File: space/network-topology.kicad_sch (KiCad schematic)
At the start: 14 parts

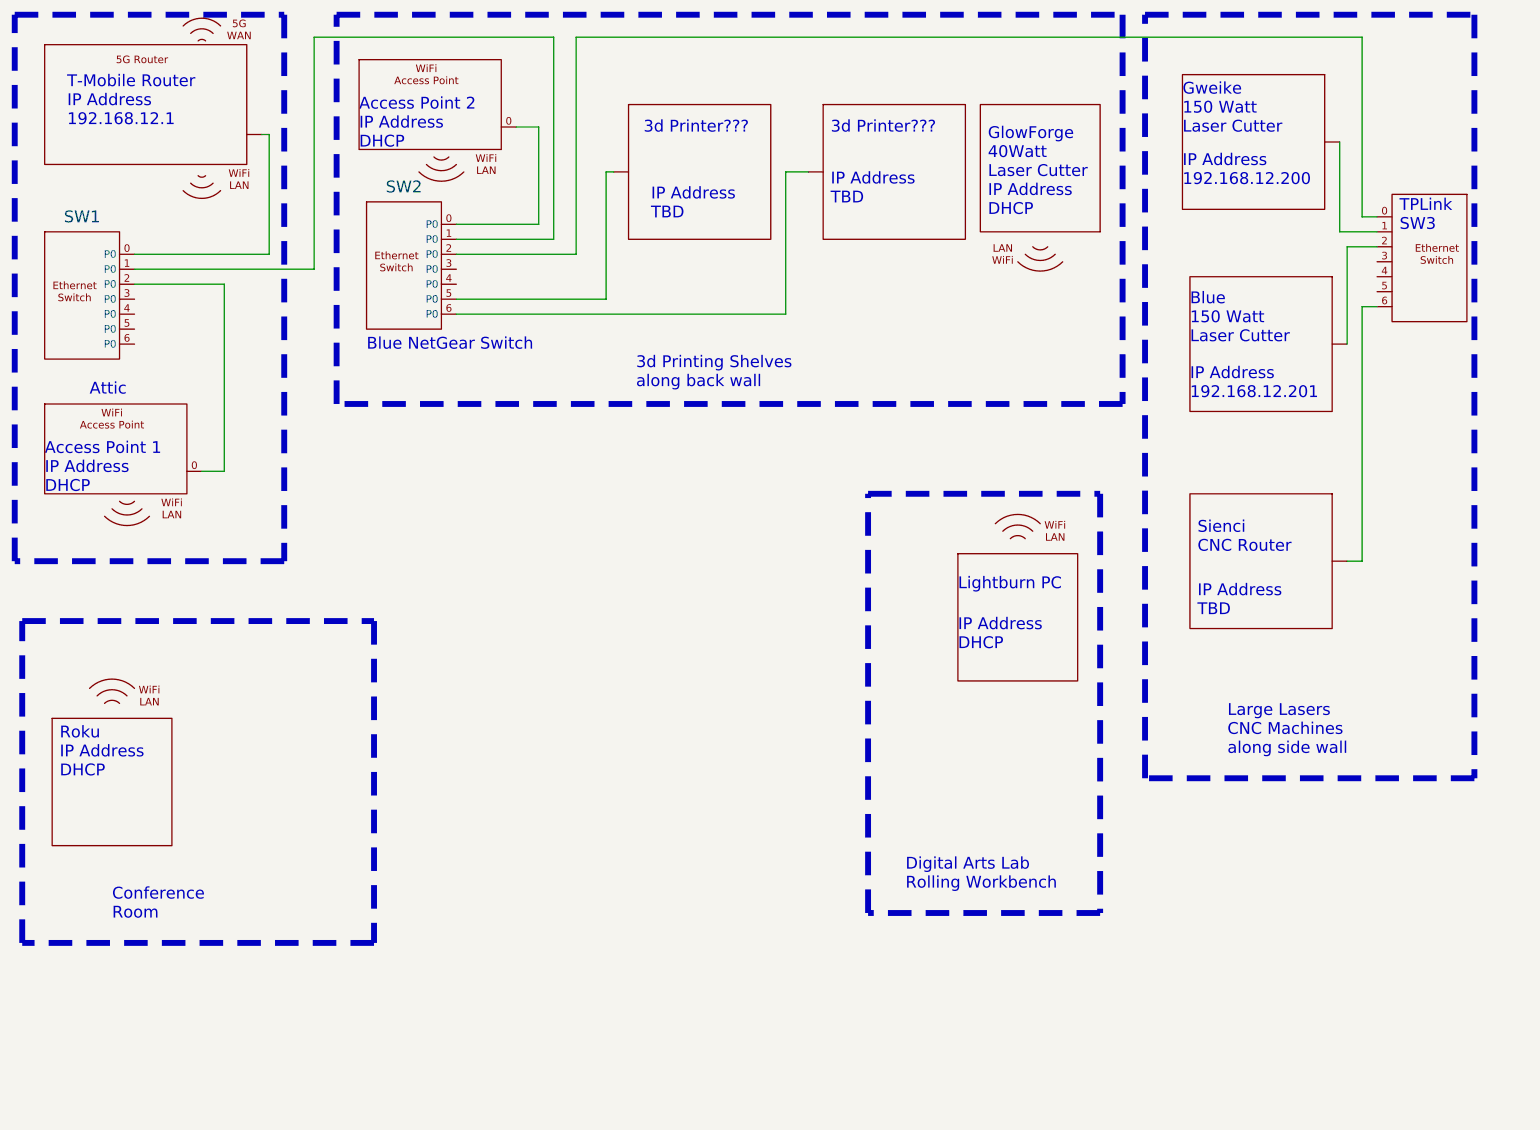
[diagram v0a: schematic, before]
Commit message: Added network map diagrams.
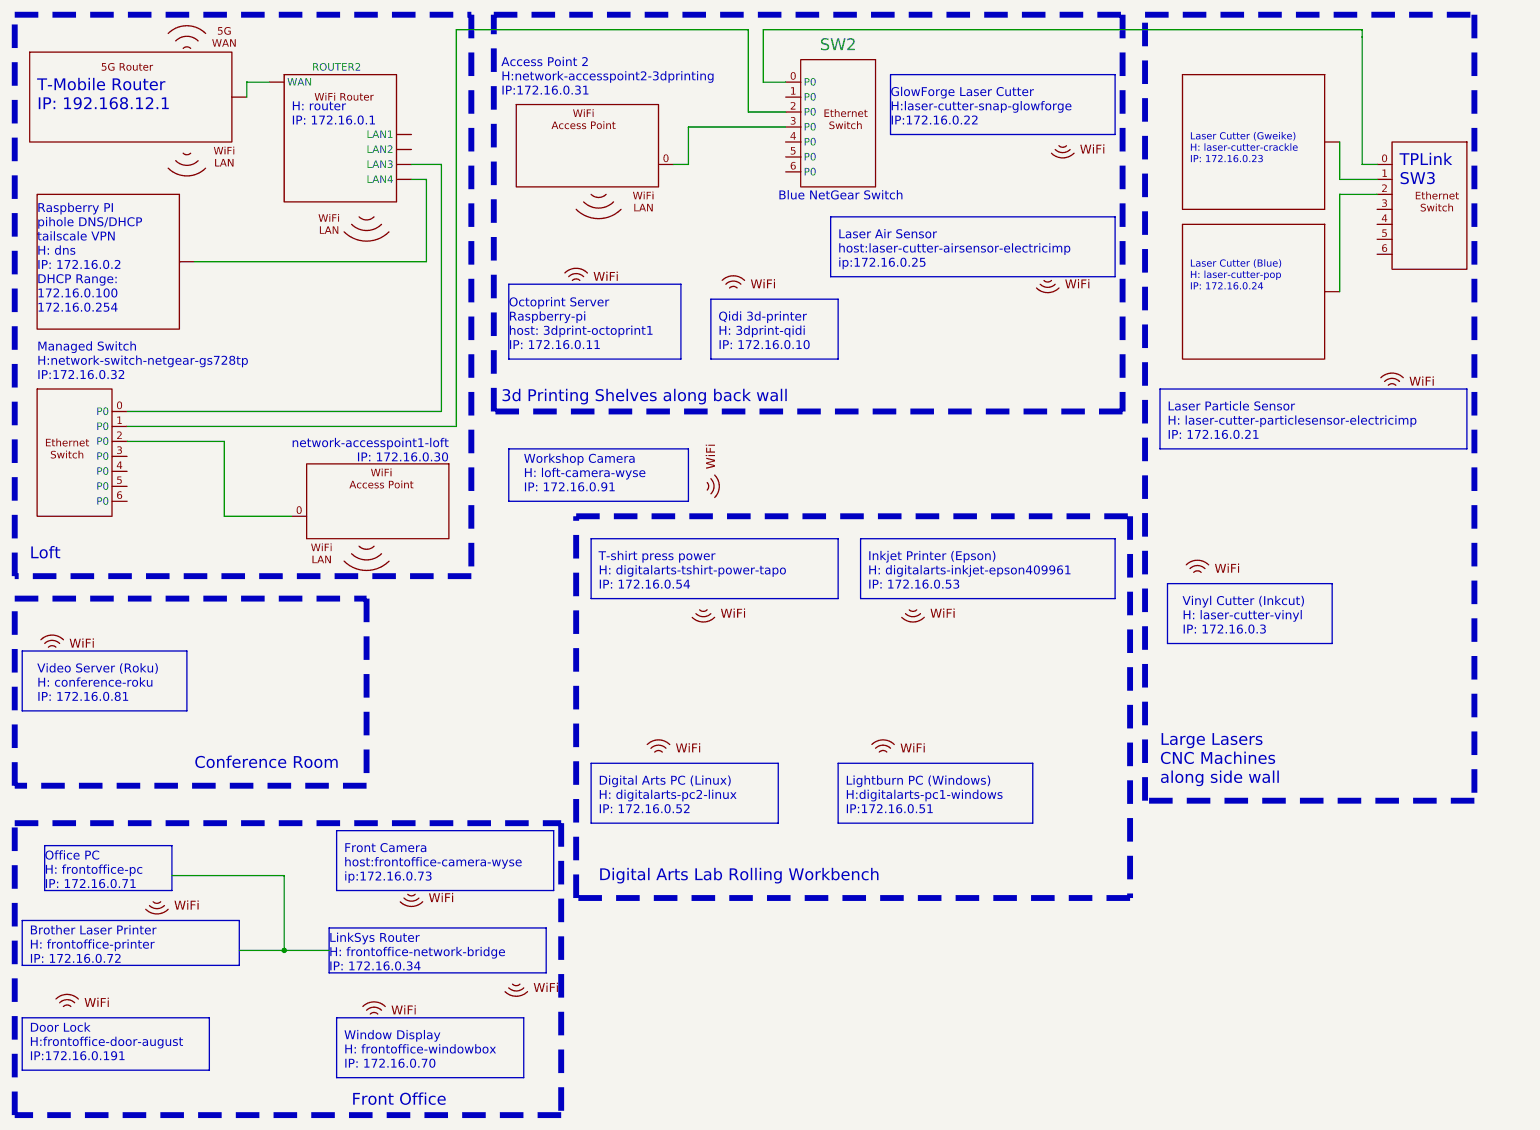
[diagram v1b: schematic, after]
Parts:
- removed U10, U9, UX: ~, symbol Networking:WiFi_Device
- removed U6, U7, U8: ~, symbol Networking:Ethernet_Device
- added DHCP/DNS: ~, symbol Networking:Ethernet_Device
- added ROUTER2: ~, symbol Networking:Wifi_Router
- added U10, U11, U13, U14, U15, U16, U17, U18, U19, U20, U21, U22, U23, U6, U7, U8, U9: ~, symbol Networking:WiFi
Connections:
- net at U1.: now also ROUTER2. (WAN); no longer SW1.0 (P0)
- net at SW2.0 (P0): now also U12.0; no longer U3.0
- net at SW2.1 (P0): no longer SW1.1 (P0)
- net at SW2.2 (P0): now also SW1.1 (P0); no longer U12.0
- net at SW2.3 (P0): now also U3.0
- new net: ROUTER2. (WAN), SW1.0 (P0)
- new net: DHCP/DNS., ROUTER2. (WAN)
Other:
- note added: "Access Point 2 H:network-accesspoint2-3dprinting IP:172.16.0.31"
- note added: "Brother Laser Printer H: frontoffice-printer IP: 172.16.0.72"
- note added: "Digital Arts PC (Linux) H: digitalarts-pc2-linux IP: 172.16.0.52"
- note added: "Door Lock H:frontoffice-door-august IP:172.16.0.191"
- note added: "Front Camera host:frontoffice-camera-wyse ip:172.16.0.73"
- note added: "Front Office"
- note added: "GlowForge Laser Cutter H:laser-cutter-snap-glowforge IP:172.16.0.22"
- note added: "H: router IP: 172.16.0.1"
- note added: "Inkjet Printer (Epson) H: digitalarts-inkjet-epson409961 IP: 172.16.0.53"
- note added: "Laser Air Sensor host:laser-cutter-airsensor-electricimp ip:172.16.0.25"
- note added: "Laser Cutter (Blue) H: laser-cutter-pop IP: 172.16.0.24"
- note added: "Laser Cutter (Gweike) H: laser-cutter-crackle IP: 172.16.0.23"
- note added: "Laser Particle Sensor H: laser-cutter-particlesensor-electricimp IP: 172.16.0.21"
- note added: "Lightburn PC (Windows) H:digitalarts-pc1-windows IP:172.16.0.51"
- note added: "LinkSys Router H: frontoffice-network-bridge IP: 172.16.0.34"
- note added: "Loft"
- note added: "Managed Switch H:network-switch-netgear-gs728tp IP:172.16.0.32"
- note added: "Octoprint Server Raspberry-pi host: 3dprint-octoprint1 IP: 172.16.0.11"
- note added: "Office PC H: frontoffice-pc IP: 172.16.0.71"
- note added: "Qidi 3d-printer H: 3dprint-qidi IP: 172.16.0.10"
- note added: "Raspberry PI pihole DNS/DHCP tailscale VPN H: dns IP: 172.16.0.2 DHCP Range: 172.16.0.100 172.16.0.254"
- note added: "T-Mobile Router IP: 192.168.12.1"
- note added: "T-shirt press power H: digitalarts-tshirt-power-tapo IP: 172.16.0.54"
- note added: "Video Server (Roku) H: conference-roku IP: 172.16.0.81"
- note added: "Vinyl Cutter (Inkcut) H: laser-cutter-vinyl IP: 172.16.0.3"
- note added: "Window Display H: frontoffice-windowbox IP: 172.16.0.70"
- note added: "Workshop Camera H: loft-camera-wyse IP: 172.16.0.91"
- note added: "network-accesspoint1-loft IP: 172.16.0.30"
- note removed: "3d Printer???"
- note removed: "Access Point 1 IP Address DHCP"
- note removed: "Access Point 2 IP Address DHCP"
- note removed: "Attic"
- note removed: "Blue 150 Watt Laser Cutter"
- note removed: "GlowForge 40Watt Laser Cutter IP Address DHCP"
- note removed: "Gweike 150 Watt Laser Cutter"
- note removed: "IP Address 192.168.12.200"
- note removed: "IP Address 192.168.12.201"
- note removed: "IP Address DHCP"
- note removed: "IP Address TBD"
- note removed: "Lightburn PC"
- note removed: "Roku IP Address DHCP"
- note removed: "Sienci CNC Router"
- note removed: "T-Mobile Router IP Address 192.168.12.1"
- title: Spark Network Map -> Spark Studio Network Map
- moved on the sheet: SW2

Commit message: Fixed label on linksys switch.
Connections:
- net at ROUTER2. (WAN): now also DHCP/DNS.
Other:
- note added: "LinSYS SW3"
- note removed: "TPLink SW3"
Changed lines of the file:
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@@
     (effects (font (size 1.5 1.5)) (justify left bottom))
   )
-  (text "TPLink\nSW3" (at 250.19 44.45 0)
+  (text "LinSYS\nSW3" (at 250.19 44.45 0)
     (effects (font (size 2 2)) (justify left bottom))
   )
